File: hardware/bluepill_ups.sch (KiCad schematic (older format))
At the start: 2 parts, among them J1 Conn_01x02

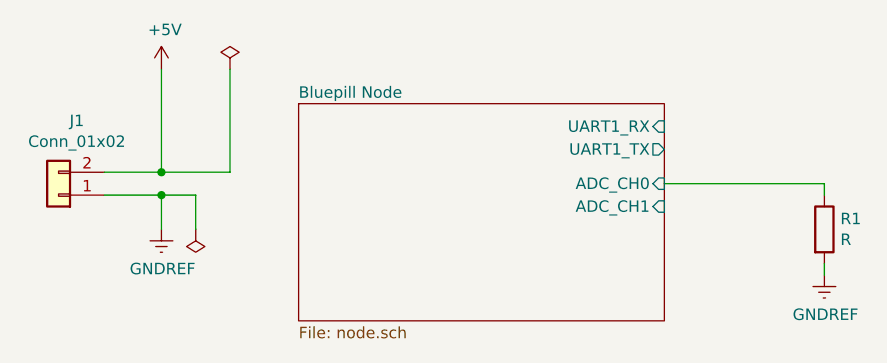
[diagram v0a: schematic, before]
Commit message: Add vero desgin to hardware
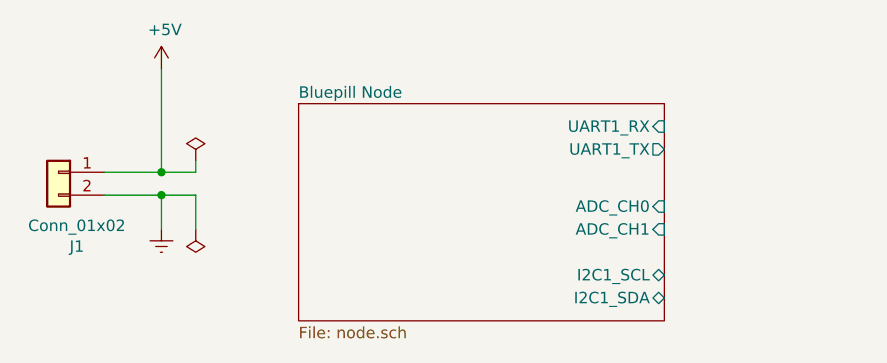
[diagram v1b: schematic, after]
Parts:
- removed R1: R, symbol Device:R
- J1: footprint (none) -> SIP2
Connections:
- net +5V: now also J1.1 (Pin_1); no longer J1.2 (Pin_2)
- net GNDREF: now also J1.2 (Pin_2); no longer J1.1 (Pin_1)
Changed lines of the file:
@@
 EESchema Schematic File Version 4
+LIBS:bluepill_ups-cache
 EELAYER 26 0
 EELAYER END
@@
 F0 "Bluepill Node" 50
 F1 "node.sch" 50
-F2 "ADC_CH0" I R 4350 2900 50
-F3 "ADC_CH1" I R 4350 3000 50
+F2 "ADC_CH0" I R 4350 3000 50
+F3 "ADC_CH1" I R 4350 3100 50
 F4 "UART1_RX" I R 4350 2650 50
 F5 "UART1_TX" O R 4350 2750 50
+F6 "I2C1_SCL" B R 4350 3300 50
+F7 "I2C1_SDA" B R 4350 3400 50
 $EndSheet
 $Comp
 L Connector_Generic:Conn_01x02 J1
 U 1 1 5C14C190
-P 1700 2950
-F 0 "J1" H 1620 2625 50  0000 C CNN
-F 1 "Conn_01x02" H 1620 2716 50  0000 C CNN
-F 2 "" H 1700 2950 50  0001 C CNN
-F 3 "~" H 1700 2950 50  0001 C CNN
-	1    1700 2950
-	-1   0    0    1
+P 1700 2850
+F 0 "J1" H 1620 2525 50  0000 C CNN
+F 1 "Conn_01x02" H 1620 2616 50  0000 C CNN
+F 2 "SIP2" H 1700 2850 50  0001 C CNN
+F 3 "~" H 1700 2850 50  0001 C CNN
+	1    1700 2850
+	-1   0    0    -1
 $EndComp
 $Comp
@@
 Wire Wire Line
 	2150 2400 2150 2850
-Wire Wire Line
-	2150 2850 1900 2850
 $Comp
 L power:GNDREF #PWR0110
@@
 P 2150 3100
 F 0 "#PWR0110" H 2150 2850 50  0001 C CNN
-F 1 "GNDREF" H 2155 2927 50  0000 C CNN
+F 1 "GNDREF" H 2155 2927 50  0001 C CNN
 F 2 "" H 2150 3100 50  0001 C CNN
 F 3 "" H 2150 3100 50  0001 C CNN
@@
 $EndComp
 Wire Wire Line
-	1900 2950 2150 2950
-Wire Wire Line
 	2150 2950 2150 3100
 $Comp
 L power:PWR_FLAG #FLG0101
 U 1 1 5C14C2D0
-P 2450 2400
-F 0 "#FLG0101" H 2450 2475 50  0001 C CNN
-F 1 "PWR_FLAG" H 2450 2574 50  0001 C CNN
-F 2 "" H 2450 2400 50  0001 C CNN
-F 3 "~" H 2450 2400 50  0001 C CNN
-	1    2450 2400
+P 2300 2800
+F 0 "#FLG0101" H 2300 2875 50  0001 C CNN
+F 1 "PWR_FLAG" H 2300 2974 50  0001 C CNN
+F 2 "" H 2300 2800 50  0001 C CNN
+F 3 "~" H 2300 2800 50  0001 C CNN
+	1    2300 2800
 	1    0    0    -1
 $EndComp
 Wire Wire Line
-	2450 2400 2450 2850
+	2300 2800 2300 2850
 Wire Wire Line
-	2450 2850 2150 2850
-Connection ~ 2150 2850
+	2300 2850 2150 2850
 $Comp
 L power:PWR_FLAG #FLG0102
@@
 Wire Wire Line
 	2300 2950 2150 2950
+Wire Wire Line
+	1900 2850 2150 2850
+Connection ~ 2150 2850
+Wire Wire Line
+	2150 2950 1900 2950
 Connection ~ 2150 2950
-$Comp
-L Device:R R1
-U 1 1 5C151FA3
-P 5050 3100
-F 0 "R1" H 5120 3146 50  0000 L CNN
-F 1 "R" H 5120 3055 50  0000 L CNN
-F 2 "" V 4980 3100 50  0001 C CNN
-F 3 "~" H 5050 3100 50  0001 C CNN
-	1    5050 3100
-	1    0    0    -1
-$EndComp
-$Comp
-L power:GNDREF #PWR01
-U 1 1 5C152039
-P 5050 3300
-F 0 "#PWR01" H 5050 3050 50  0001 C CNN
-F 1 "GNDREF" H 5055 3127 50  0000 C CNN
-F 2 "" H 5050 3300 50  0001 C CNN
-F 3 "" H 5050 3300 50  0001 C CNN
-	1    5050 3300
-	1    0    0    -1
-$EndComp
-Wire Wire Line
-	5050 3250 5050 3300
-Wire Wire Line
-	5050 2950 5050 2900
-Wire Wire Line
-	5050 2900 4350 2900
 $EndSCHEMATC

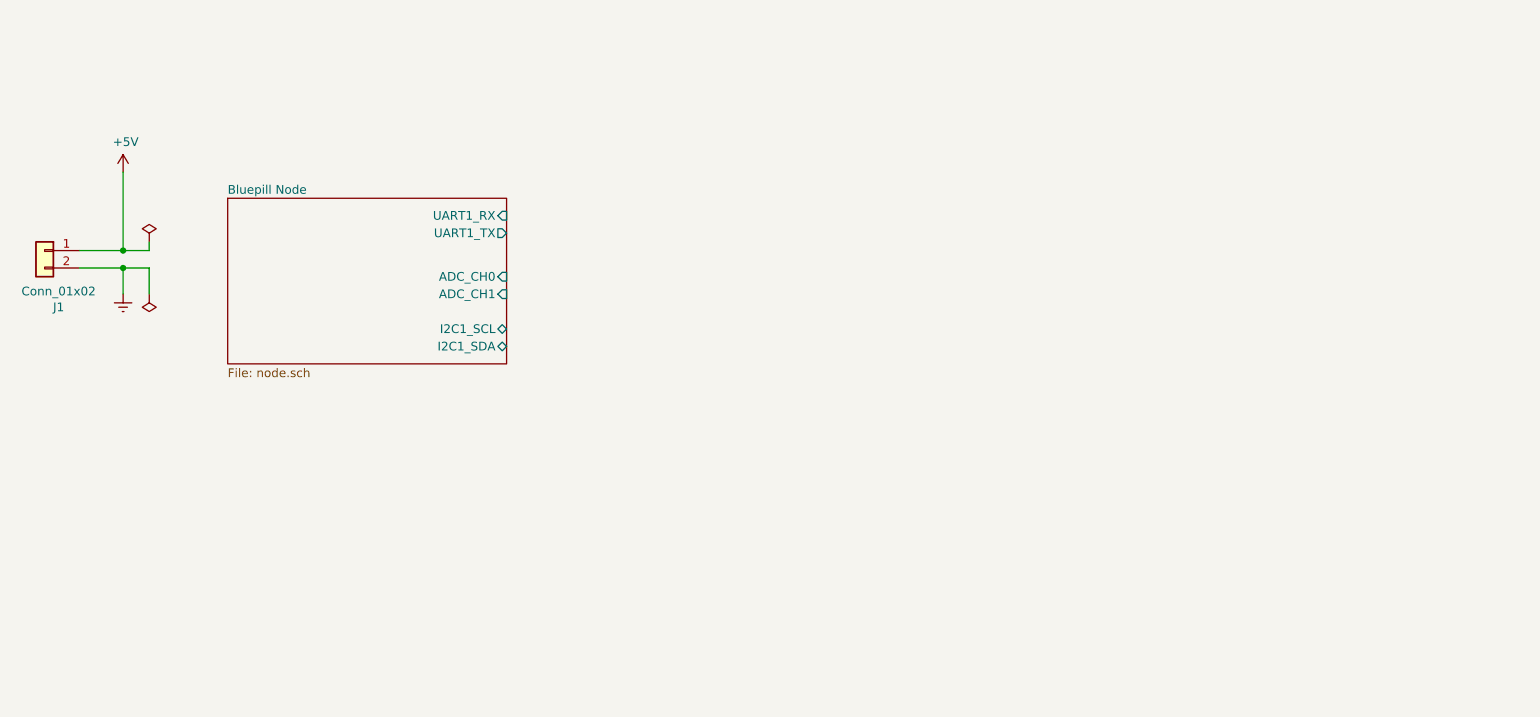
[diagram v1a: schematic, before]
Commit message: Move both UPS to this node
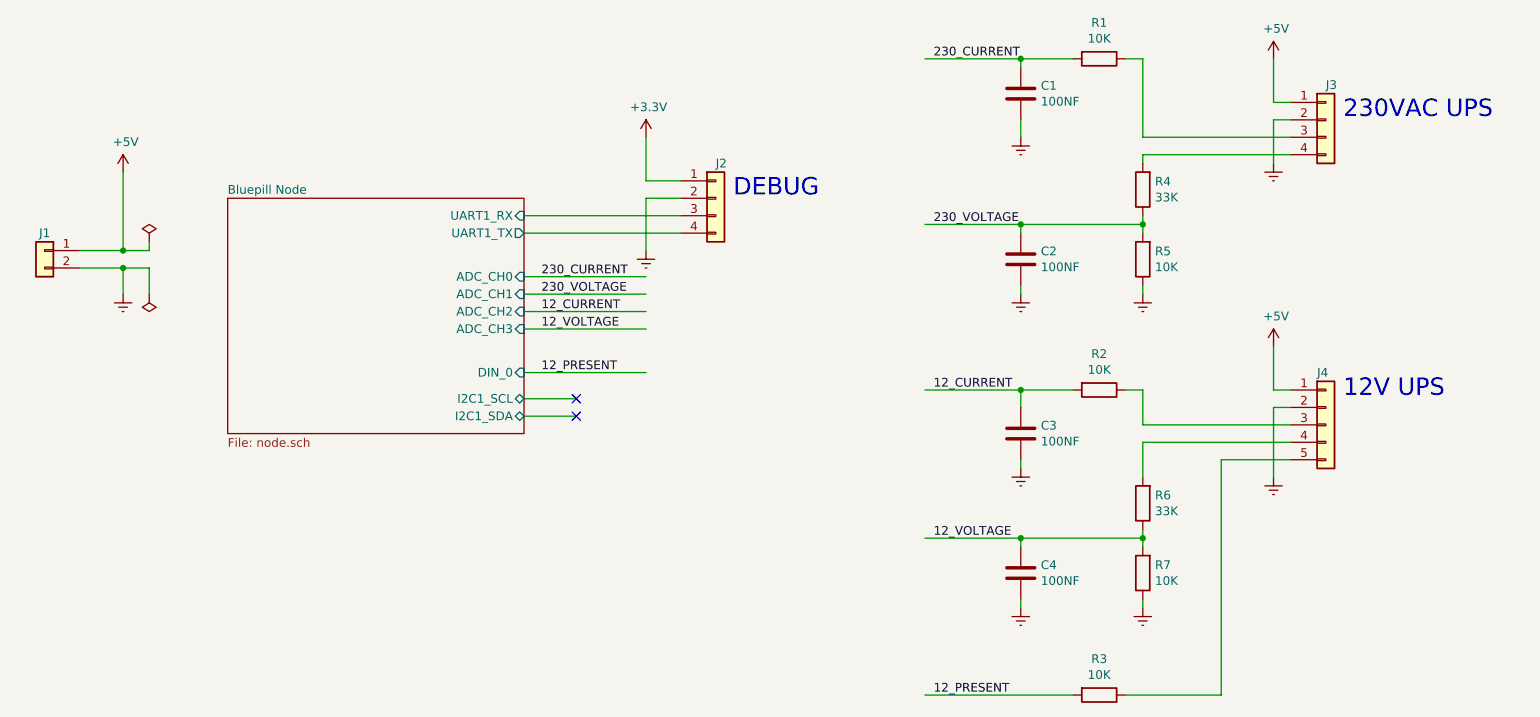
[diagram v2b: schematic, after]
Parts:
- added C1, C2, C3, C4: 100NF, symbol Device:C
- added J2, J3: Conn_01x04, symbol Connector_Generic:Conn_01x04
- added J4: Conn_01x05, symbol Connector_Generic:Conn_01x05
- added R1, R2, R3, R5, R7: 10K, symbol Device:R
- added R4, R6: 33K, symbol Device:R
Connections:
- net labels added: +3.3V, 12_CURRENT, 12_PRESENT, 12_VOLTAGE, 230_CURRENT, 230_VOLTAGE
- wire segments 8 -> 65
- no-connect marks 0 -> 2
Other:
- note added: "12V UPS"
- note added: "230VAC UPS"
- note added: "DEBUG"
